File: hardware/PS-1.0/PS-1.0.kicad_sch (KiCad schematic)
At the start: 50 parts, among them J5 Conn_01x04, J8 Conn_01x03, J9 Conn_01x03, K1 RAYEX-L90, K2 RAYEX-L90, Q1 IRFPE50, Q2 IRFPE50, Q3 IRFPE50, U1 TC4422

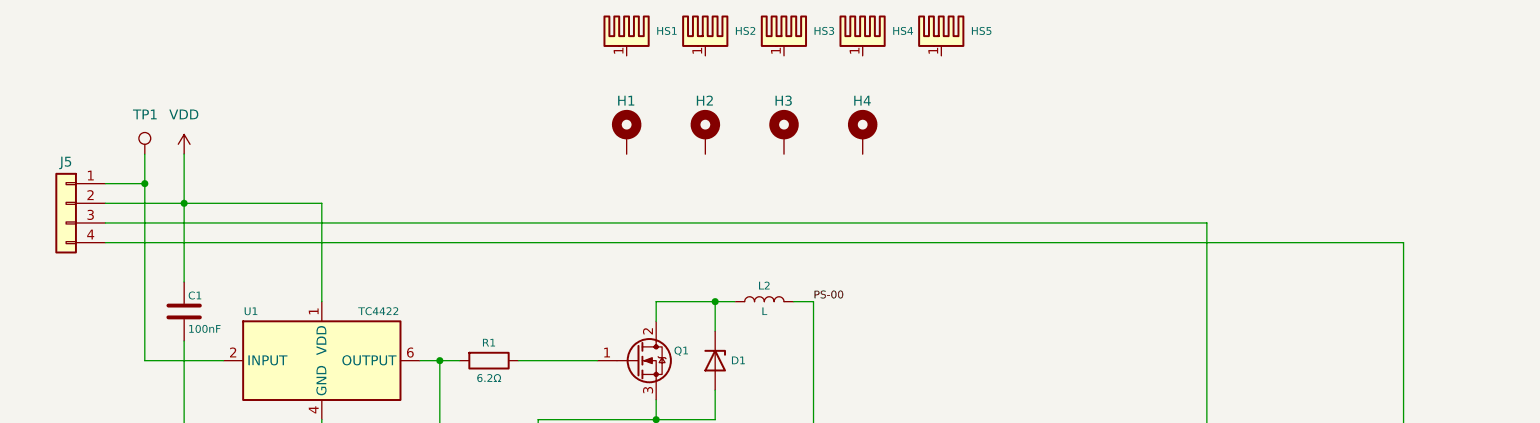
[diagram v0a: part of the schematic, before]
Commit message: new file:   hardware/Gain/Gain-B_Cu.gbr 	new file:   hardware/Gain/Gain-B_Mask.gbr 	new file:   hardware/Gain/Gain-B_Paste.gbr 	new file:   hardware/Gain/Gain-B_Silkscreen.gbr 	new file:   hardware/Gain/Gain-Edge_Cuts.gbr 	new file:   hardware/Gain/Gain-F_Cu.gbr 	new file:   hardware/Gain/Gain-F_Mask.gbr 	new file:   hardware/Gain/Gain-F_Paste.gbr 	new file:   hardware/Gain/Gain-F_Silkscreen.gbr 	new file:   hardware/Gain/Gain-NPTH.drl 	new file:   hardware/Gain/Gain-PTH.drl 	new file:   hardware/Gain/Gain-backups/Gain-2025-04-14_115147.zip 	new file:   hardware/Gain/Gain-backups/Gain-2025-04-14_121847.zip 	new file:   hardware/Gain/Gain-backups/Gain-2025-04-14_133755.zip 	new file:   hardware/Gain/Gain-backups/Gain-2025-04-14_141907.zip 	new file:   hardware/Gain/Gain-backups/Gain-2025-04-14_162042.zip 	new file:   hardware/Gain/Gain-backups/Gain-2025-04-14_163456.zip 	new file:   hardware/Gain/Gain-job.gbrjob 	new file:   hardware/Gain/Gain.kicad_pcb 	new file:   hardware/Gain/Gain.kicad_prl 	new file:   hardware/Gain/Gain.kicad_pro 	new file:   hardware/Gain/Gain.kicad_sch 	new file:   hardware/Gain/Gain.step 	new file:   hardware/Gain/REM-2.0 BoM.csv 	new file:   hardware/Gain/REM-2.0-backups/REM-2.0-2025-03-05_160217.zip 	new file:   hardware/Gain/REM-2.0-backups/REM-2.0-2025-03-06_081735.zip 	new file:   hardware/Gain/REM-2.0-backups/REM-2.0-2025-03-17_111724.zip 	new file:   hardware/Gain/REM-2.0-backups/REM-2.0-2025-03-17_135033.zip 	new file:   hardware/Gain/REM-2.0-backups/REM-2.0-2025-03-18_104019.zip 	new file:   hardware/Gain/REM-2.0-backups/REM-2.0-2025-03-18_141720.zip 	new file:   hardware/Gain/REM-2.0-backups/REM-2.0-2025-03-18_202240.zip 	new file:   hardware/Gain/REM-2.0-backups/REM-2.0-2025-03-18_203414.zip 	new file:   hardware/Gain/REM-2.0-backups/REM-2.0-2025-03-18_204444.zip 	new file:   hardware/Gain/REM-2.0-backups/REM-2.0-2025-03-24_102406.zip 	new file:   hardware/Gain/REM-2.0-backups/REM-2.0-2025-03-24_103843.zip 	new file:   hardware/Ga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
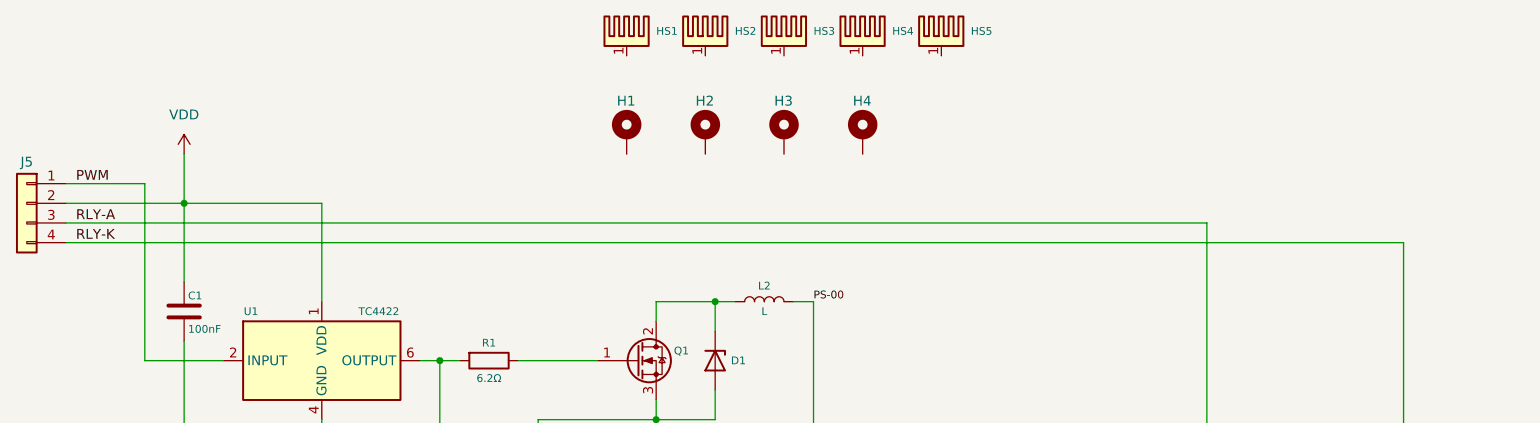
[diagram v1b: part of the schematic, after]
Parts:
- removed TP1: TestPoint, TestPoint:TestPoint_Bridge_Pitch2.54mm_Drill1.0mm, symbol Connector:TestPoint
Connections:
- net PWM: now reaches J5.1 (Pin_1), U1.2 (INPUT)
- net RLY-A: now reaches D8.1 (K), D9.1 (K), J5.3 (Pin_3), K1.A2, K2.A2
- net RLY-K: now reaches D8.2 (A), D9.2 (A), J5.4 (Pin_4), K1.A1, K2.A1
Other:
- moved on the sheet: J5
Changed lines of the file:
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@@
-	)
-	(junction
-		(at 66.04 48.26)
-		(diameter 0)
-		(color 0 0 0 0)
 	)
 	(junction
@@
 	(wire
 		(pts
-			(xy 60.96 50.8) (xy 71.12 50.8)
+			(xy 55.88 50.8) (xy 71.12 50.8)
 		)
 		(stroke
@@
 	(wire
 		(pts
-			(xy 60.96 53.34) (xy 203.2 53.34)
+			(xy 55.88 53.34) (xy 203.2 53.34)
 		)
 		(stroke
@@
 	(wire
 		(pts
-			(xy 228.6 55.88) (xy 60.96 55.88)
+			(xy 228.6 55.88) (xy 55.88 55.88)
 		)
 		(stroke
@@
 	(wire
 		(pts
-			(xy 66.04 44.45) (xy 66.04 48.26)
-		)
-		(stroke
-			(width 0)
-			(type default)
-		)
-	)
-	(wire
-		(pts
 			(xy 66.04 48.26) (xy 66.04 71.12)
 		)
@@
 	(wire
 		(pts
-			(xy 60.96 48.26) (xy 66.04 48.26)
+			(xy 55.88 48.26) (xy 66.04 48.26)
 		)
 		(stroke
@@
 			(width 0)
 			(type default)
+		)
+	)
+	(label "RLY-A"
+		(at 57.15 53.34 0)
+		(fields_autoplaced yes)
+		(effects
+			(font
+				(size 1.27 1.27)
+			)
+			(justify left bottom)
 		)
 	)
@@
 			(font
 				(size 1 1)
+			)
+			(justify left bottom)
+		)
+	)
+	(label "PWM"
+		(at 57.15 48.26 0)
+		(fields_autoplaced yes)
+		(effects
+			(font
+				(size 1.27 1.27)
+			)
+			(justify left bottom)
+		)
+	)
+	(label "RLY-K"
+		(at 57.15 55.88 0)
+		(fields_autoplaced yes)
+		(effects
+			(font
+				(size 1.27 1.27)
 			)
 			(justify left bottom)
@@
 	(symbol
 		(lib_id "Connector_Generic:Conn_01x04")
-		(at 55.88 50.8 0)
+		(at 50.8 50.8 0)
 		(mirror y)
 		(unit 1)
@@
 		(dnp no)
 		(property "Reference" "J5"
-			(at 55.88 45.466 0)
+			(at 50.8 45.466 0)
 			(effects
 				(font
@@
 		)
 		(property "Value" "Conn_01x04"
-			(at 55.88 44.45 0)
+			(at 50.8 44.45 0)
 			(effects
 				(font
@@
 		)
 		(property "Footprint" "Connector_PinHeader_2.54mm:PinHeader_1x04_P2.54mm_Vertical"
-			(at 55.88 50.8 0)
+			(at 50.8 50.8 0)
 			(effects
 				(font
@@
 		)
 		(property "Datasheet" "~"
-			(at 55.88 50.8 0)
+			(at 50.8 50.8 0)
 			(effects
 				(font
@@
 		)
 		(property "Description" "Generic connector, single row, 01x04, script generated (kicad-library-utils/schlib/autogen/connector/)"
-			(at 55.88 50.8 0)
+			(at 50.8 50.8 0)
 			(effects
 				(font
@@
 					(unit 1)
 				)
-			)
-		)
-	)
-	(symbol
-		(lib_id "Connector:TestPoint")
-		(at 66.04 44.45 0)
-		(unit 1)
-		(exclude_from_sim no)
-		(in_bom yes)
-		(on_board yes)
-		(dnp no)
-		(property "Reference" "TP1"
-			(at 64.516 39.37 0)
-			(effects
-				(font
-					(size 1.27 1.27)
-				)
-				(justify left)
-			)
-		)
-		(property "Value" "TestPoint"
-			(at 68.58 43.6879 0)
-			(effects
-				(font
-					(size 1.27 1.27)
-				)
-				(justify left)
-				(hide yes)
-			)
-		)
-		(property "Footprint" "TestPoint:TestPoint_Bridge_Pitch2.54mm_Drill1.0mm"
-			(at 71.12 44.45 0)
-			(effects
-				(font
-					(size 1.27 1.27)
-				)
-				(hide yes)
-			)
-		)
-		(property "Datasheet" "~"
-			(at 71.12 44.45 0)
-			(effects
-				(font
-					(size 1.27 1.27)
-				)
-				(hide yes)
-			)
-		)
-		(property "Description" "test point"
-			(at 66.04 44.45 0)
-			(effects
-				(font
-					(size 1.27 1.27)
-				)
-				(hide yes)
-			)
-		)
-		(pin "1"
-		)
-		(instances
-			(project ""
-				(path "/3a4da535-700d-4512-9d93-355e5c375ab5"
-					(reference "TP1")
-					(unit 1)
-				)

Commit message: deleted:    hardware/Gain/Gain-backups/Gain-2025-04-14_115147.zip 	new file:   hardware/Gain/Gain-backups/Gain-2025-04-15_120154.zip 	deleted:    hardware/MSD-1.0/MSD-1.0-backups/MSD-1.0-2025-03-24_134332.zip 	deleted:    hardware/MSD-1.0/MSD-1.0-backups/MSD-1.0-2025-03-25_144744.zip 	deleted:    hardware/MSD-1.0/MSD-1.0-backups/MSD-1.0-2025-03-25_145433.zip 	deleted:    hardware/MSD-1.0/MSD-1.0-backups/MSD-1.0-2025-03-25_150210.zip 	deleted:    hardware/MSD-1.0/MSD-1.0-backups/MSD-1.0-2025-03-25_150818.zip 	new file:   hardware/MSD-1.0/MSD-1.0-backups/MSD-1.0-2025-04-16_142822.zip 	new file:   hardware/MSD-1.0/MSD-1.0-backups/MSD-1.0-2025-04-16_143722.zip 	new file:   hardware/MSD-1.0/MSD-1.0-backups/MSD-1.0-2025-04-16_145208.zip 	new file:   hardware/MSD-1.0/MSD-1.0-backups/MSD-1.0-2025-04-16_150237.zip 	new file:   hardware/MSD-1.0/MSD-1.0-backups/MSD-1.0-2025-04-16_150829.zip 	modified:   hardware/MSD-1.0/MSD-1.0.kicad_pcb 	modified:   hardware/MSD-1.0/MSD-1.0.kicad_sch 	modified:   hardware/MSD-1.0/MSD-1.0.step 	new file:   hardware/MSD-2.0/MSD-2.0-backups/MSD-2.0-2025-04-16_090248.zip 	deleted:    hardware/PS-1.0/PS-1.0-backups/PS-1.0-2025-03-18_205016.zip 	deleted:    hardware/PS-1.0/PS-1.0-backups/PS-1.0-2025-03-18_205728.zip 	deleted:    hardware/PS-1.0/PS-1.0-backups/PS-1.0-2025-03-18_211157.zip 	deleted:    hardware/PS-1.0/PS-1.0-backups/PS-1.0-2025-03-18_213933.zip 	deleted:    hardware/PS-1.0/PS-1.0-backups/PS-1.0-2025-03-19_094557.zip 	deleted:    hardware/PS-1.0/PS-1.0-backups/PS-1.0-2025-03-19_101204.zip 	deleted:    hardware/PS-1.0/PS-1.0-backups/PS-1.0-2025-03-19_102323.zip 	new file:   hardware/PS-1.0/PS-1.0-backups/PS-1.0-2025-04-16_154157.zip 	new file:   hardware/PS-1.0/PS-1.0-backups/PS-1.0-2025-04-16_154838.zip 	new file:   hardware/PS-1.0/PS-1.0-backups/PS-1.0-2025-04-16_155906.zip 	new file:   hardware/PS-1.0/PS-1.0-backups/PS-1.0-2025-04-16_160456.zip 	new file:   hardware/PS-1.0/PS-1.0-backups/PS-1.0-2025-04-16_161300.zip 	new file:   har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
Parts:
- removed HS1, HS2, HS3: Heatsink_Pad, Heatsink:Heatsink_Fischer_SK129-STS_42x25mm_2xDrill2.5mm, symbol Mechanical:Heatsink_Pad
- removed HS4, HS5: Heatsink_Pad, Heatsink:Heatsink_Stonecold_HS-132_32x14mm_2xFixation1.5mm, symbol Mechanical:Heatsink_Pad
- removed J5: Conn_01x04, Connector_PinHeader_2.54mm:PinHeader_1x04_P2.54mm_Vertical, symbol Connector_Generic:Conn_01x04
- added J1: Conn_02x16_Odd_Even, Connector_PinSocket_2.54mm:PinSocket_2x16_P2.54mm_Vertical, symbol Connector_Generic:Conn_02x16_Odd_Even
- added J2, J3: Conn_01x05, Connector_Molex:Molex_KK-396_5273-05A_1x05_P3.96mm_Vertical_2, symbol Connector_Generic:Conn_01x05
- U3: footprint Custom:ESU-MSD-1.0 -> Custom:ESU-REM-3.0
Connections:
- net PWM: now also J1.2 (Pin_2)
- net RLY-A: now also D8.2 (A), D9.2 (A), K1.A1, K2.A1, J1.6 (Pin_6); no longer D8.1 (K), D9.1 (K), K1.A2, K2.A2
- net RLY-K: now also D8.1 (K), D9.1 (K), K1.A2, K2.A2, J1.8 (Pin_8); no longer D8.2 (A), D9.2 (A), K1.A1, K2.A1
- net VDD: now also J1.4 (Pin_4)
- new net: J1.10 (Pin_10), U2.1 (5V), U3.1 (5V)
- new net: J1.12 (Pin_12), U2.2 (GND), U3.2 (GND)
- new net: J1.14 (Pin_14), U3.3 (OUT1)
- new net: J1.16 (Pin_16), U3.4 (OUT2)
- new net: J1.18 (Pin_18), U2.4 (OUT)
- new net: J2.1 (Pin_1), U2.5 (COM)
- new net: J2.3 (Pin_3), U2.6 (PAD2)
- new net: J2.5 (Pin_5), U2.7 (PAD1)
- new net: J3.1 (Pin_1), U3.5 (IN1)
- new net: J3.3 (Pin_3), U3.6 (IN2)
- new net: J3.5 (Pin_5), U3.7 (COM)
